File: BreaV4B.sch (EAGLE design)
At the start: 32 parts, among them J1 XF2L-0535-1, J2 XF2L-0535-1, Q3 ABM-16MHZ, SW1 ESE31L11T, SW2 EVQ11U09K, SW3 LS12T2-T, U1 TPS62200, X1 22-23-2021

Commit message: TrussKey Schematics
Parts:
- R8: value 10K -> 1K
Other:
- note added: "0.9V VOUT"
- note added: "Detection"
- note added: "FPC"
- note added: "LED"
- note added: "Power"
- note added: "Programmer"
- note added: "Solenoid"

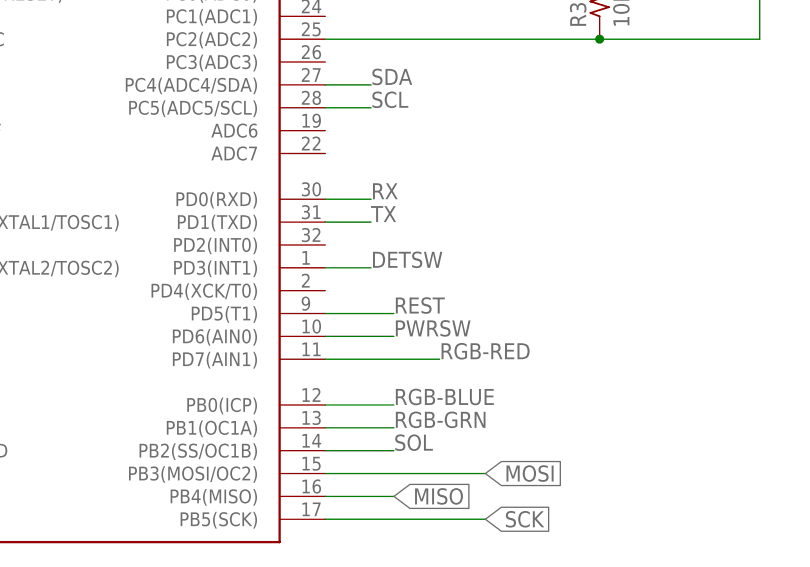
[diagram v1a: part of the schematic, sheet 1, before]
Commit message: Power Switch to int0
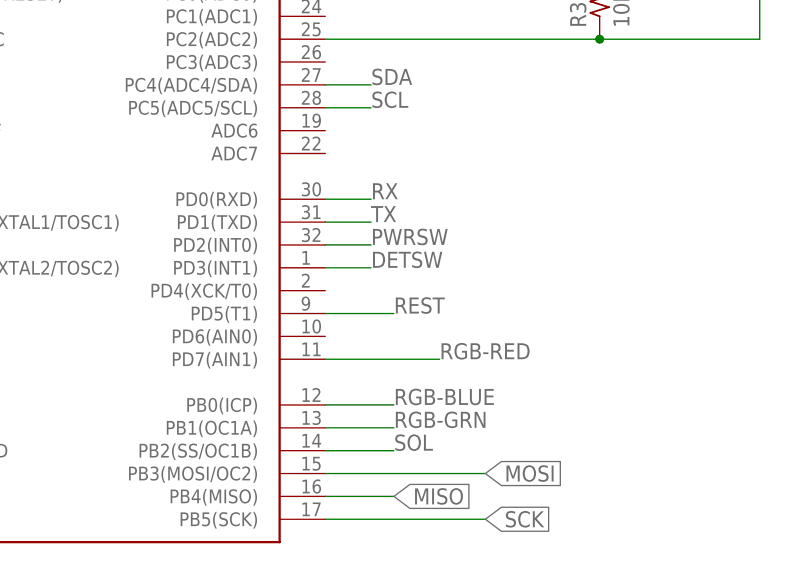
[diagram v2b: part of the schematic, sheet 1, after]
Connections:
- net PWRSW: now also U2.PD2(INT0); no longer U2.PD6(AIN0)
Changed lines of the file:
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@@
-</segment>
-</net>
-<net name="PWRSW" class="0">
-<segment>
-<pinref part="U2" gate="U$1" pin="PD6(AIN0)"/>
-<wire x1="86.36" y1="43.18" x2="93.98" y2="43.18" width="0.1524" layer="91"/>
-<label x="93.98" y="43.18" size="1.778" layer="95"/>
 </segment>
 </net>
@@
 </segment>
 </net>
+<net name="PWRSW" class="0">
+<segment>
+<pinref part="U2" gate="U$1" pin="PD2(INT0)"/>
+<wire x1="86.36" y1="53.34" x2="91.44" y2="53.34" width="0.1524" layer="91"/>
+<label x="91.44" y="53.34" size="1.778" layer="95"/>
+</segment>
+</net>

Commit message: Rx Tx
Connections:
- net RX: now also J1-4.MS; no longer J1-3.MS
- net TX: now also J1-3.MS; no longer J1-4.MS
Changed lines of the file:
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@@
-</segment>
-</net>
-<net name="RX" class="0">
-<segment>
-<pinref part="J1" gate="-3" pin="MS"/>
-<wire x1="160.02" y1="93.98" x2="147.32" y2="93.98" width="0.1524" layer="91"/>
-<label x="147.32" y="93.98" size="1.778" layer="95"/>
-</segment>
-</net>
-<net name="TX" class="0">
-<segment>
-<pinref part="J1" gate="-4" pin="MS"/>
-<wire x1="160.02" y1="91.44" x2="147.32" y2="91.44" width="0.1524" layer="91"/>
-<label x="144.78" y="91.44" size="1.778" layer="95"/>
 </segment>
 </net>
@@
 </segment>
 </net>
+<net name="RX" class="0">
+<segment>
+<pinref part="J1" gate="-4" pin="MS"/>
+<wire x1="160.02" y1="91.44" x2="147.32" y2="91.44" width="0.1524" layer="91"/>
+<label x="147.32" y="91.44" size="1.778" layer="95"/>
+</segment>
+</net>
+<net name="TX" class="0">
+<segment>
+<pinref part="J1" gate="-3" pin="MS"/>
+<wire x1="160.02" y1="93.98" x2="147.32" y2="93.98" width="0.1524" layer="91"/>
+<label x="147.32" y="93.98" size="1.778" layer="95"/>
+</segment>
+</net>
